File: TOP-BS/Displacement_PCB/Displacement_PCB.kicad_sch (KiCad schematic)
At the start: 2 parts

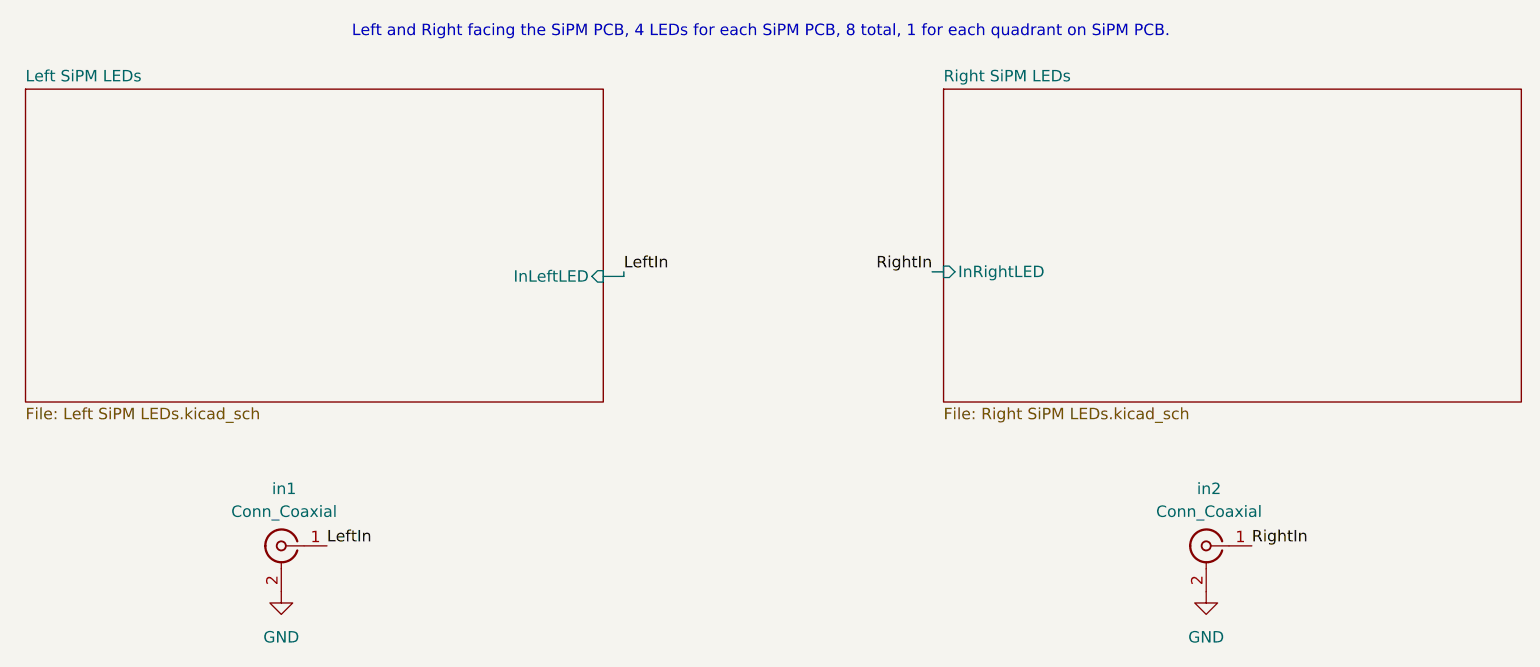
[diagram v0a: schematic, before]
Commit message: Updated Distribution PCB sch
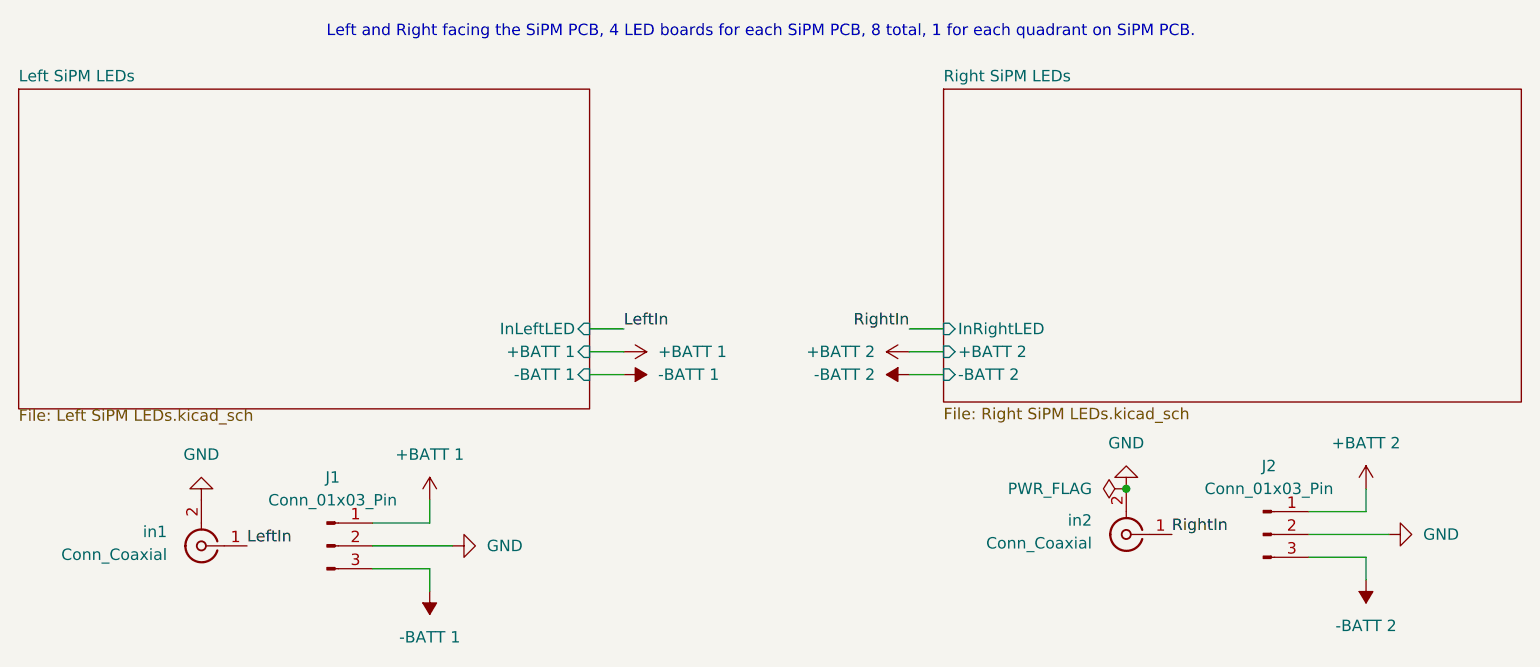
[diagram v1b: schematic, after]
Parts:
- added J1, J2: Conn_01x03_Pin, kicad-mza:molex-mini-fit-jr-3pos-right-angle-or-16AWG, symbol Connector:Conn_01x03_Pin
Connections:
- net GND: now also J1.2 (Pin_2), J2.2 (Pin_2)
- new net +BATT 1: J1.1 (Pin_1)
- new net +BATT 2: J2.1 (Pin_1)
- new net -BATT 1: J1.3 (Pin_3)
- new net -BATT 2: J2.3 (Pin_3)
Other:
- sheet Left SiPM LEDs ports: added +BATT 1, -BATT 1; removed none
- sheet Right SiPM LEDs ports: added +BATT 2, -BATT 2; removed none
- note added: "Left and Right facing the SiPM PCB, 4 LED boards for each SiPM PCB, 8 total, 1 for each quadrant on SiPM PCB."
- note removed: "Left and Right facing the SiPM PCB, 4 LEDs for each SiPM PCB, 8 total, 1 for each quadrant on SiPM PCB."
